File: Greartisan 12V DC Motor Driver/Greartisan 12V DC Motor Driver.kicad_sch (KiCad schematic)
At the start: 4 parts, among them M1 Motor_DC, M2 Motor_DC, U1 L298N

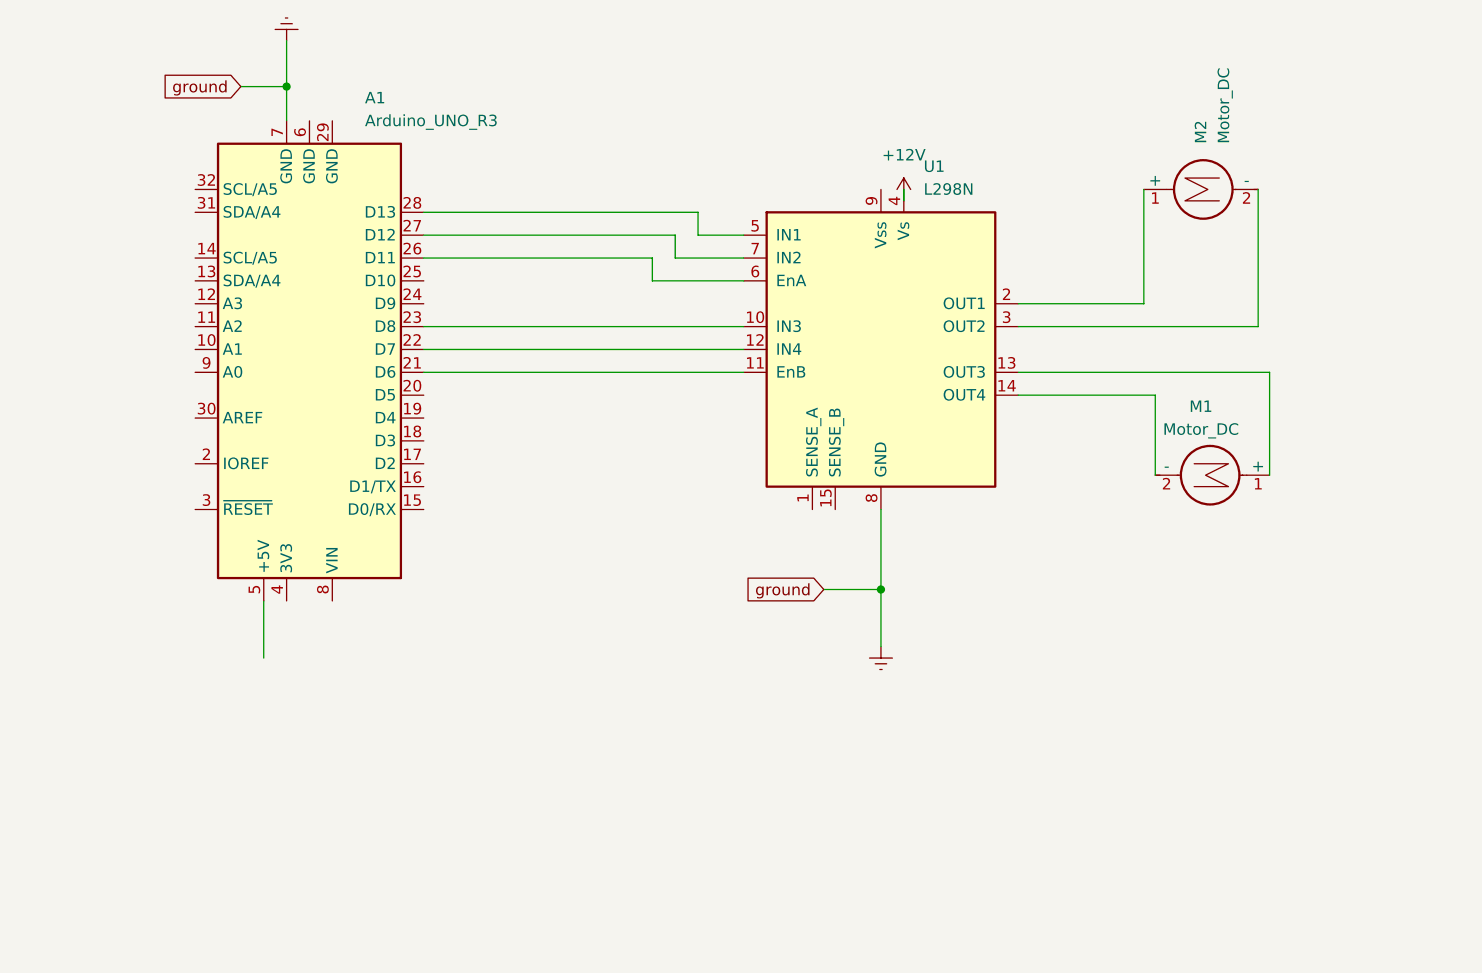
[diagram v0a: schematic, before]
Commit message: added voltage regulator
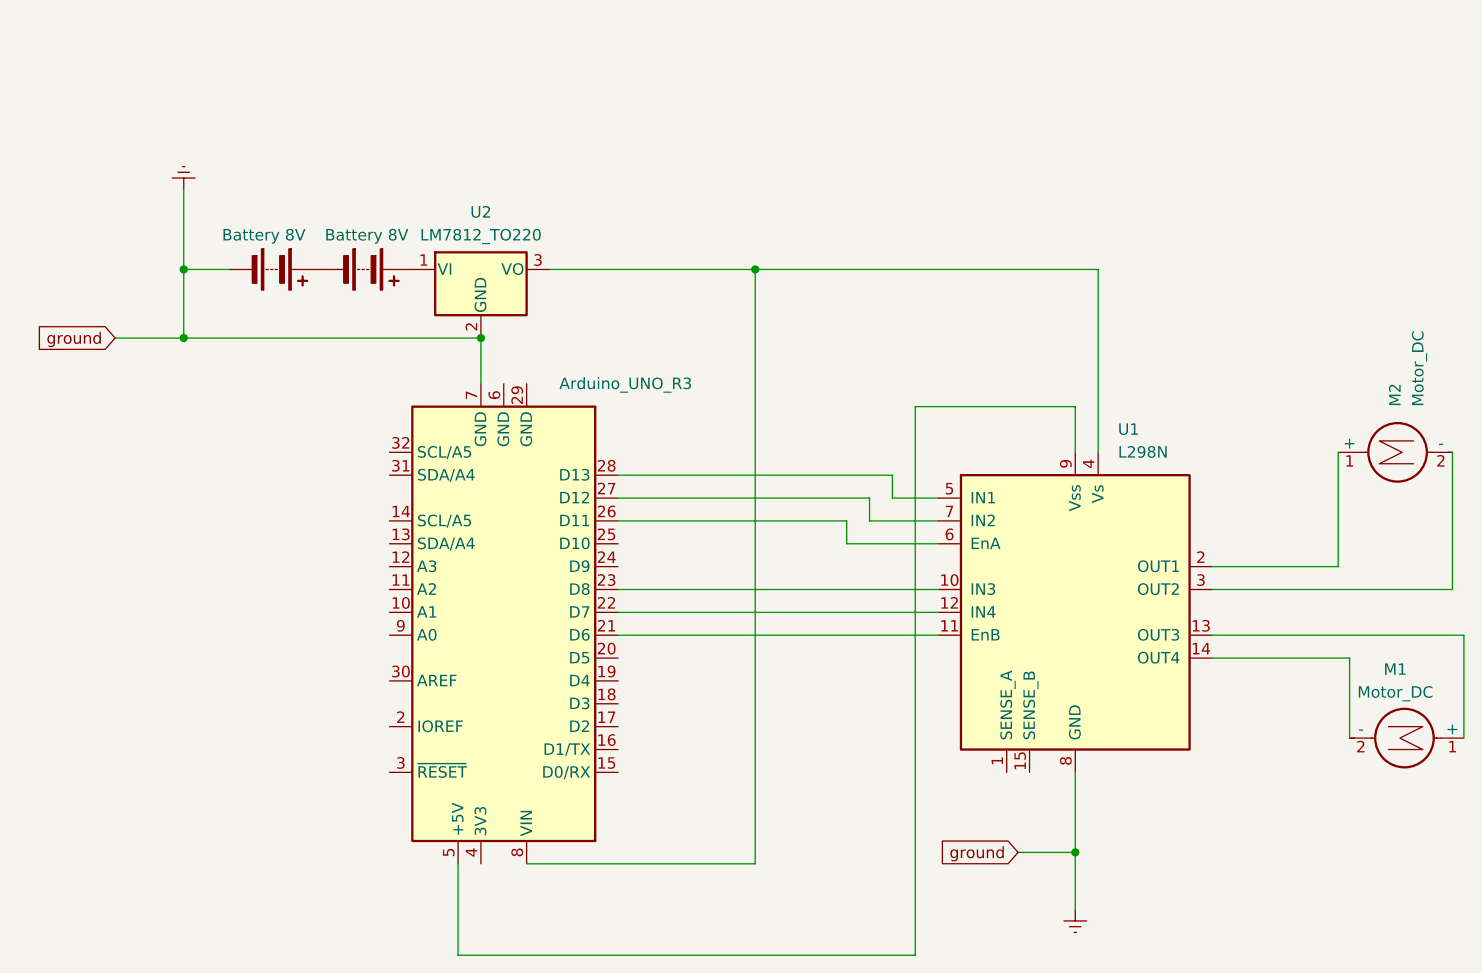
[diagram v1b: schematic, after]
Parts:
- added BT1, BT2: Battery 8V, symbol Device:Battery
- added U2: LM7812_TO220, Package_TO_SOT_THT:TO-220-3_Vertical, symbol Regulator_Linear:LM7812_TO220
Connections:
- net +12V is gone; now on an unnamed net: U1.4 (Vs)
- net Earth: now also BT1.2 (-), U2.2 (GND)
- net at A1.5 (+5V): now also U1.9 (Vss)
- net at A1.8 (VIN): now also U2.3 (VO)
- new net: BT1.1 (+), BT2.2 (-)
- new net: BT2.1 (+), U2.1 (VI)
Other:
- moved on the sheet: M1, M2, U1
